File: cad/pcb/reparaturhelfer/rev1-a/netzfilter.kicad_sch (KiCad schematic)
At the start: 6 parts, among them J501 Conn_01x03

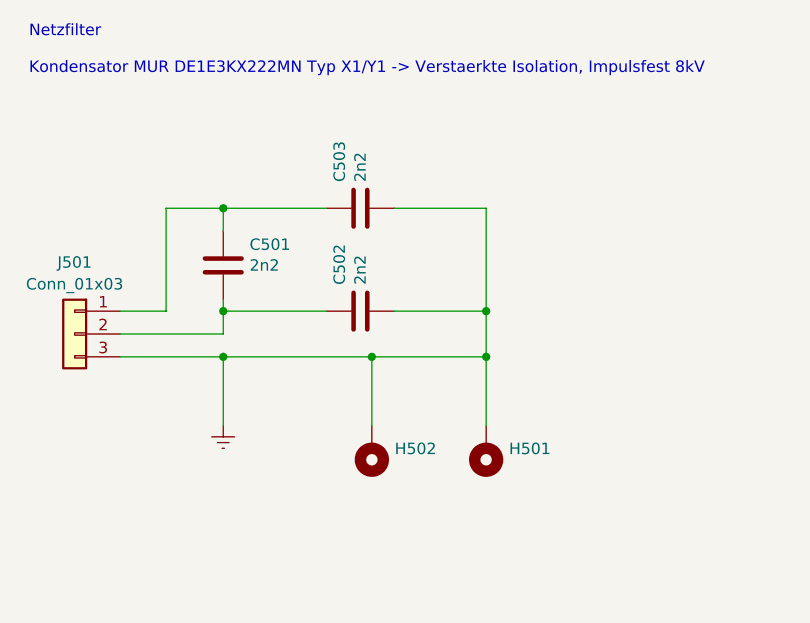
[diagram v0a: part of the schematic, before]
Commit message: Add: Routing Bluetooth
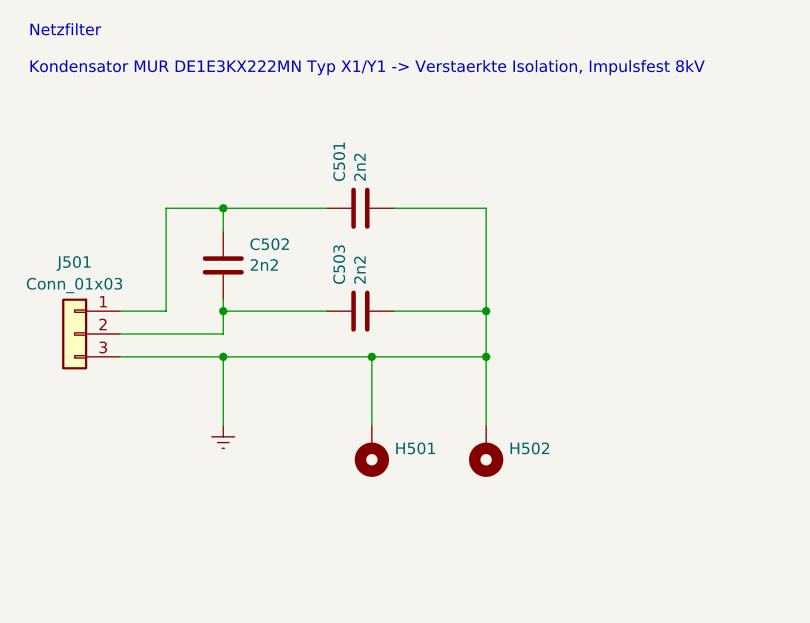
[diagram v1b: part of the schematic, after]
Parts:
- J501: footprint (none) -> Connector_PinHeader_2.54mm:PinHeader_1x03_P2.54mm_Vertical
- renumbered C503 to C501, C501 to C502, C502 to C503, H502 to H501, H501 to H502
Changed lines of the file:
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@@
   (symbol (lib_id "Device:C") (at 74.93 55.88 90) (unit 1)
     (in_bom yes) (on_board yes) (dnp no)
-    (property "Reference" "C502" (at 72.6186 52.959 0)
+    (property "Reference" "C503" (at 72.6186 52.959 0)
       (effects (font (size 1.27 1.27)) (justify left))
     )
@@
       (project "reparaturhelfer"
         (path "/93378ebd-f9ac-4734-8bdd-78f97f3ae344/4327f5a1-8aa2-42ba-9107-de0665ca43c2"
-          (reference "C502") (unit 1)
+          (reference "C503") (unit 1)
         )
       )
@@
   (symbol (lib_id "Mechanical:MountingHole_Pad") (at 88.9 71.12 180) (unit 1)
     (in_bom yes) (on_board yes) (dnp no) (fields_autoplaced)
-    (property "Reference" "H501" (at 91.44 71.1779 0)
+    (property "Reference" "H502" (at 91.44 71.1779 0)
       (effects (font (size 1.27 1.27)) (justify right))
     )
@@
       (project "reparaturhelfer"
         (path "/93378ebd-f9ac-4734-8bdd-78f97f3ae344/4327f5a1-8aa2-42ba-9107-de0665ca43c2"
-          (reference "H501") (unit 1)
+          (reference "H502") (unit 1)
         )
       )
@@
   (symbol (lib_id "Device:C") (at 59.69 50.8 0) (unit 1)
     (in_bom yes) (on_board yes) (dnp no)
-    (property "Reference" "C501" (at 62.611 48.4886 0)
+    (property "Reference" "C502" (at 62.611 48.4886 0)
       (effects (font (size 1.27 1.27)) (justify left))
     )
@@
       (project "reparaturhelfer"
         (path "/93378ebd-f9ac-4734-8bdd-78f97f3ae344/4327f5a1-8aa2-42ba-9107-de0665ca43c2"
-          (reference "C501") (unit 1)
+          (reference "C502") (unit 1)
         )
       )
@@
       (effects (font (size 1.27 1.27)))
     )
-    (property "Footprint" "" (at 43.18 58.42 0)
+    (property "Footprint" "Connector_PinHeader_2.54mm:PinHeader_1x03_P2.54mm_Vertical" (at 43.18 58.42 0)
       (effects (font (size 1.27 1.27)) hide)
     )
@@
   (symbol (lib_id "Device:C") (at 74.93 44.45 90) (unit 1)
     (in_bom yes) (on_board yes) (dnp no)
-    (property "Reference" "C503" (at 72.6186 41.529 0)
+    (property "Reference" "C501" (at 72.6186 41.529 0)
       (effects (font (size 1.27 1.27)) (justify left))
     )
@@
       (project "reparaturhelfer"
         (path "/93378ebd-f9ac-4734-8bdd-78f97f3ae344/4327f5a1-8aa2-42ba-9107-de0665ca43c2"
-          (reference "C503") (unit 1)
+          (reference "C501") (unit 1)
         )
       )
@@
   (symbol (lib_id "Mechanical:MountingHole_Pad") (at 76.2 71.12 180) (unit 1)
     (in_bom yes) (on_board yes) (dnp no) (fields_autoplaced)
-    (property "Reference" "H502" (at 78.74 71.1779 0)
+    (property "Reference" "H501" (at 78.74 71.1779 0)
       (effects (font (size 1.27 1.27)) (justify right))
     )
@@
       (project "reparaturhelfer"
         (path "/93378ebd-f9ac-4734-8bdd-78f97f3ae344/4327f5a1-8aa2-42ba-9107-de0665ca43c2"
-          (reference "H502") (unit 1)
+          (reference "H501") (unit 1)
         )
       )

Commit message: Add: PCB fertig
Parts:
- removed H502: MountingHole_Pad, MountingHole:MountingHole_3mm_Pad, symbol Mechanical:MountingHole_Pad
- added H502: MountingHole, MountingHole:MountingHole_3.2mm_M3, symbol Mechanical:MountingHole
- H501: footprint MountingHole:MountingHole_3mm_Pad -> MountingHole:MountingHole_3.2mm_M3_Pad
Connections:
- net Earth: no longer J501.3 (Pin_3)
- net at C502.2, C503.1: now also J501.3 (Pin_3); no longer J501.2 (Pin_2)
- no-connect marks 0 -> 1
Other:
- moved on the sheet: H501
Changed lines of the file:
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@@
     (comment 2 "Erweiterung um Bluetooth.")
   )
-  (junction (at 76.2 60.96) (diameter 0) (color 0 0 0 0)
+  (junction (at 88.9 55.88) (diameter 0) (color 0 0 0 0)
   )
   (junction (at 88.9 60.96) (diameter 0) (color 0 0 0 0)
   )
-  (junction (at 88.9 55.88) (diameter 0) (color 0 0 0 0)
-  )
   (junction (at 59.69 44.45) (diameter 0) (color 0 0 0 0)
   )
-  (junction (at 59.69 60.96) (diameter 0) (color 0 0 0 0)
-  )
   (junction (at 59.69 55.88) (diameter 0) (color 0 0 0 0)
   )
+  (no_connect (at 48.26 58.42))
+  (wire (pts (xy 59.69 54.61) (xy 59.69 55.88))
+    (stroke (width 0) (type default))
+  )
+  (wire (pts (xy 59.69 55.88) (xy 59.69 60.96))
+    (stroke (width 0) (type default))
+  )
+  (wire (pts (xy 78.74 55.88) (xy 88.9 55.88))
+    (stroke (width 0) (type default))
+  )
+  (wire (pts (xy 48.26 55.88) (xy 53.34 55.88))
+    (stroke (width 0) (type default))
+  )
+  (wire (pts (xy 53.34 44.45) (xy 59.69 44.45))
+    (stroke (width 0) (type default))
+  )
+  (wire (pts (xy 88.9 55.88) (xy 88.9 60.96))
+    (stroke (width 0) (type default))
+  )
+  (wire (pts (xy 59.69 55.88) (xy 71.12 55.88))
+    (stroke (width 0) (type default))
+  )
   (wire (pts (xy 48.26 60.96) (xy 59.69 60.96))
     (stroke (width 0) (type default))
   )
-  (wire (pts (xy 59.69 54.61) (xy 59.69 55.88))
-    (stroke (width 0) (type default))
-  )
-  (wire (pts (xy 59.69 55.88) (xy 59.69 58.42))
-    (stroke (width 0) (type default))
-  )
-  (wire (pts (xy 78.74 55.88) (xy 88.9 55.88))
-    (stroke (width 0) (type default))
-  )
-  (wire (pts (xy 59.69 60.96) (xy 76.2 60.96))
-    (stroke (width 0) (type default))
-  )
-  (wire (pts (xy 48.26 55.88) (xy 53.34 55.88))
-    (stroke (width 0) (type default))
-  )
-  (wire (pts (xy 53.34 44.45) (xy 59.69 44.45))
-    (stroke (width 0) (type default))
-  )
-  (wire (pts (xy 88.9 55.88) (xy 88.9 60.96))
-    (stroke (width 0) (type default))
-  )
-  (wire (pts (xy 88.9 68.58) (xy 88.9 60.96))
-    (stroke (width 0) (type default))
-  )
-  (wire (pts (xy 59.69 55.88) (xy 71.12 55.88))
-    (stroke (width 0) (type default))
-  )
   (wire (pts (xy 59.69 44.45) (xy 71.12 44.45))
     (stroke (width 0) (type default))
@@
     (stroke (width 0) (type default))
   )
-  (wire (pts (xy 59.69 60.96) (xy 59.69 68.58))
+  (wire (pts (xy 88.9 60.96) (xy 88.9 68.58))
     (stroke (width 0) (type default))
   )
@@
     (stroke (width 0) (type default))
   )
-  (wire (pts (xy 76.2 60.96) (xy 76.2 68.58))
-    (stroke (width 0) (type default))
-  )
-  (wire (pts (xy 59.69 58.42) (xy 48.26 58.42))
+  (wire (pts (xy 76.2 60.96) (xy 76.2 67.31))
     (stroke (width 0) (type default))
   )
@@
     (effects (font (size 1.27 1.27)) (justify left bottom))
   )
-  (symbol (lib_id "power:Earth") (at 59.69 68.58 0) (unit 1)
-    (in_bom yes) (on_board yes) (dnp no) (fields_autoplaced)
-    (property "Reference" "#PWR0501" (at 59.69 74.93 0)
-      (effects (font (size 1.27 1.27)) hide)
-    )
-    (property "Value" "Earth" (at 59.69 72.39 0)
-      (effects (font (size 1.27 1.27)) hide)
-    )
-    (property "Footprint" "" (at 59.69 68.58 0)
-      (effects (font (size 1.27 1.27)) hide)
-    )
-    (property "Datasheet" "~" (at 59.69 68.58 0)
+  (symbol (lib_id "power:Earth") (at 88.9 68.58 0) (unit 1)
+    (in_bom yes) (on_board yes) (dnp no) (fields_autoplaced)
+    (property "Reference" "#PWR0501" (at 88.9 74.93 0)
+      (effects (font (size 1.27 1.27)) hide)
+    )
+    (property "Value" "Earth" (at 88.9 72.39 0)
+      (effects (font (size 1.27 1.27)) hide)
+    )
+    (property "Footprint" "" (at 88.9 68.58 0)
+      (effects (font (size 1.27 1.27)) hide)
+    )
+    (property "Datasheet" "~" (at 88.9 68.58 0)
       (effects (font (size 1.27 1.27)) hide)
     )
@@
         (path "/93378ebd-f9ac-4734-8bdd-78f97f3ae344/4327f5a1-8aa2-42ba-9107-de0665ca43c2"
           (reference "C503") (unit 1)
-        )
-      )
-    )
-  )
-  (symbol (lib_id "Mechanical:MountingHole_Pad") (at 88.9 71.12 180) (unit 1)
-    (in_bom yes) (on_board yes) (dnp no) (fields_autoplaced)
-    (property "Reference" "H502" (at 91.44 71.1779 0)
-      (effects (font (size 1.27 1.27)) (justify right))
-    )
-    (property "Value" "MountingHole_Pad" (at 91.44 73.6021 0)
-      (effects (font (size 1.27 1.27)) (justify right) hide)
-    )
-    (property "Footprint" "MountingHole:MountingHole_3mm_Pad" (at 88.9 71.12 0)
-      (effects (font (size 1.27 1.27)) hide)
-    )
-    (property "Datasheet" "~" (at 88.9 71.12 0)
-      (effects (font (size 1.27 1.27)) hide)
-    )
-    (pin "1")
-    (instances
-      (project "reparaturhelfer"
-        (path "/93378ebd-f9ac-4734-8bdd-78f97f3ae344/4327f5a1-8aa2-42ba-9107-de0665ca43c2"
-          (reference "H502") (unit 1)
         )
       )
@@
     )
   )
+  (symbol (lib_id "Mechanical:MountingHole") (at 76.2 80.01 0) (unit 1)
+    (in_bom yes) (on_board yes) (dnp no) (fields_autoplaced)
+    (property "Reference" "H502" (at 78.74 78.7979 0)
+      (effects (font (size 1.27 1.27)) (justify left))
+    )
+    (property "Value" "MountingHole" (at 78.74 81.2221 0)
+      (effects (font (size 1.27 1.27)) (justify left) hide)
+    )
+    (property "Footprint" "MountingHole:MountingHole_3.2mm_M3" (at 76.2 80.01 0)
+      (effects (font (size 1.27 1.27)) hide)
+    )
+    (property "Datasheet" "~" (at 76.2 80.01 0)
+      (effects (font (size 1.27 1.27)) hide)
+    )
+    (instances
+      (project "reparaturhelfer"
+        (path "/93378ebd-f9ac-4734-8bdd-78f97f3ae344/4327f5a1-8aa2-42ba-9107-de0665ca43c2"
+          (reference "H502") (unit 1)
+        )
+      )
+    )
+  )
   (symbol (lib_id "Graphic:Logo_Open_Hardware_Small") (at 276.86 173.99 0) (unit 1)
     (in_bom yes) (on_board yes) (dnp no)
@@
     )
   )
-  (symbol (lib_id "Mechanical:MountingHole_Pad") (at 76.2 71.12 180) (unit 1)
-    (in_bom yes) (on_board yes) (dnp no) (fields_autoplaced)
-    (property "Reference" "H501" (at 78.74 71.1779 0)
+  (symbol (lib_id "Mechanical:MountingHole_Pad") (at 76.2 69.85 180) (unit 1)
+    (in_bom yes) (on_board yes) (dnp no) (fields_autoplaced)
+    (property "Reference" "H501" (at 78.74 69.9079 0)
       (effects (font (size 1.27 1.27)) (justify right))
     )
-    (property "Value" "MountingHole_Pad" (at 78.74 73.6021 0)
+    (property "Value" "MountingHole_Pad" (at 78.74 72.3321 0)
       (effects (font (size 1.27 1.27)) (justify right) hide)
     )
-    (property "Footprint" "MountingHole:MountingHole_3mm_Pad" (at 76.2 71.12 0)
-      (effects (font (size 1.27 1.27)) hide)
-    )
-    (property "Datasheet" "~" (at 76.2 71.12 0)
-      (effects (font (size 1.27 1.27)) hide)
-    )
+    (property "Footprint" "MountingHole:MountingHole_3.2mm_M3_Pad" (at 76.2 69.85 0)
+      (effects (font (size 1.27 1.27)) hide)
+    )
+    (property "Datasheet" "~" (at 76.2 69.85 0)
+      (effects (font (size 1.27 1.27)) hide)
+    )
